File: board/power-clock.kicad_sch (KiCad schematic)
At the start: 15 parts, among them J3 AdaFruit 4090 USB-C BOB, SW1 RESET, Y4 12MHz

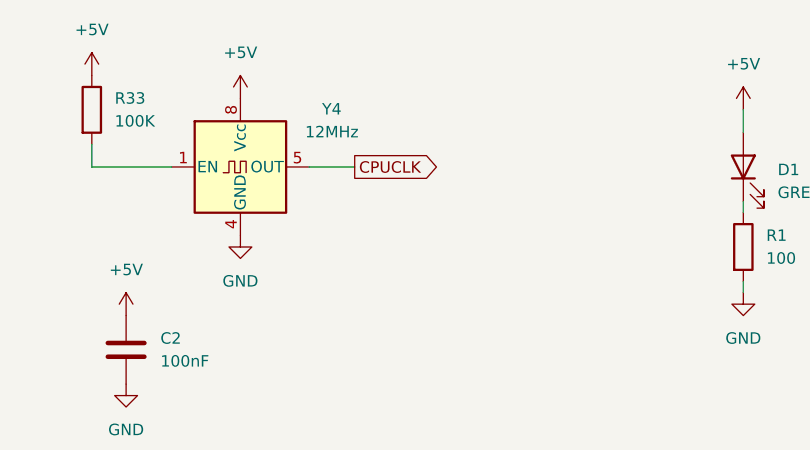
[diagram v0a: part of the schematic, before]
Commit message: CPUCLK -> SYSCLK
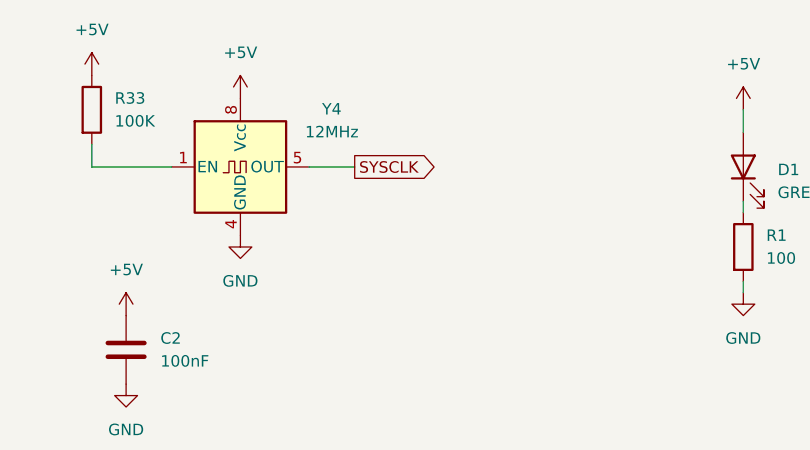
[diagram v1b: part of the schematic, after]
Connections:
- net CPUCLK renamed SYSCLK
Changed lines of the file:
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@@
 		)
 	)
-	(global_label "CPUCLK"
+	(global_label "SYSCLK"
 		(shape output)
 		(at 101.6 53.34 0)
